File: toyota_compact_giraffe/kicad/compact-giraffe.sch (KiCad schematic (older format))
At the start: 7 parts, among them J2 MOBILEEYE, J3 MOBILEEYE, P1 panda, U1 Power, U2 USB

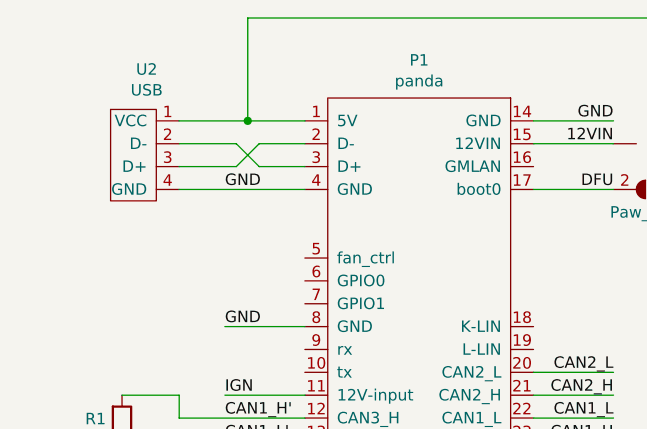
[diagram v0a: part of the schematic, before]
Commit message: modifications for v3. trace width, re-routs for easier 12v soldering
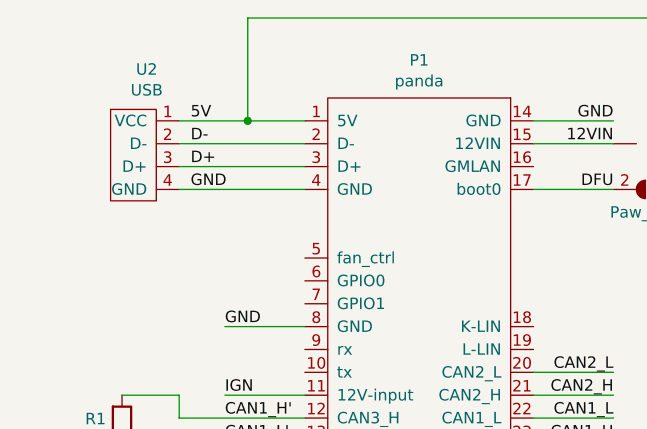
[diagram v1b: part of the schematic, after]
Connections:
- net 5V: now reaches JP1.1 (A), P1.1 (5V), U2.1 (VCC)
- net D+: now reaches U2.3 (D+)
- net D+: now also P1.3 (D+); no longer P1.2 (D-)
- net D-: now reaches U2.2 (D-)
- net D-: now also P1.2 (D-); no longer P1.3 (D+)
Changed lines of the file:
@@
 EESchema Schematic File Version 4
-LIBS:minimal-toyota-giraffe-cache
 EELAYER 29 0
 EELAYER END
@@
 Text Notes 4650 2700 0    50   ~ 0
 Const 12V\n-Comma Power\n-Mirror Pin\n-Sun Roof
-Wire Wire Line
-	2350 2700 2600 2700
-Wire Wire Line
-	2600 2700 2700 2600
-Wire Wire Line
-	2700 2600 2900 2600
-Wire Wire Line
-	2900 2700 2700 2700
-Wire Wire Line
-	2700 2700 2600 2600
-Wire Wire Line
-	2600 2600 2350 2600
 $Comp
 L giraffe:USB U2
@@
 Wire Wire Line
 	2900 3400 2550 3400
-Text Label 2550 2800 0    50   ~ 0
-GND
 Wire Wire Line
 	2350 2500 2650 2500
@@
 Wire Wire Line
 	2650 2500 2900 2500
+Wire Wire Line
+	2900 2600 2350 2600
+Wire Wire Line
+	2350 2700 2900 2700
+Text Label 2400 2800 0    50   ~ 0
+GND
+Text Label 2400 2700 0    50   ~ 0
+D+
+Text Label 2400 2600 0    50   ~ 0
+D-
+Text Label 2400 2500 0    50   ~ 0
+5V
 $EndSCHEMATC
